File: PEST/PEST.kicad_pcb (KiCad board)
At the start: 4 copper layers, 6.2 x 4.9 mm, 4 parts, among them J1 Conn_01x01, J2 Conn_01x01, J3 Conn_01x01, J4 Conn_01x01

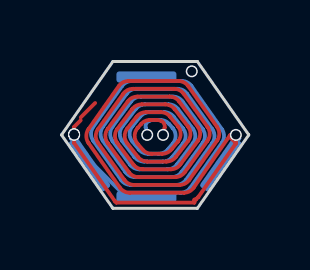
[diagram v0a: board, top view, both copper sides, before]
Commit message: Fixed some PEST tile glitches
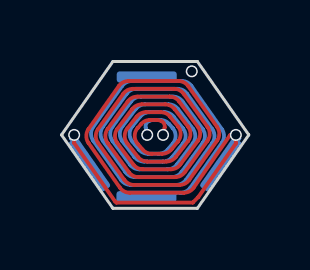
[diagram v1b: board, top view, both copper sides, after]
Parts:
- removed J3, J4: Conn_01x01, PEST:Bridge_Pad
- added J1: Conn_01x01, Touchstone:Bridge_Pad, B.Cu at (17.8, 21.0)
- added J2: Conn_01x01, Touchstone:Bridge_Pad, B.Cu at (19.7, 18.1)
- J1, J2: footprint PEST:Bridge_Pad -> Touchstone:Bridge_Pad
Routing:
- net Net-(J1-Pin_1): track 210.0 -> 206.4 mm, vias 6 -> 5
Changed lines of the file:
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@@
   (net 0 "")
   (net 1 "Net-(J1-Pin_1)")
-  (footprint "PEST:Bridge_Pad" (layer "B.Cu")
-    (at 19.71 18.07)
+  (footprint "Touchstone:Bridge_Pad" (layer "B.Cu")
+    (at 17.81 20.99 -55)
     (property "Sheetfile" "PEST.kicad_sch")
     (property "Sheetname" "")
@@
     (property "ki_keywords" "connector")
     (attr smd)
-    (fp_text reference "J4" (at -2.5 0.5 180 unlocked) (layer "B.SilkS") hide
+    (fp_text reference "J1" (at -2.5 0.5 125 unlocked) (layer "B.SilkS") hide
         (effects (font (size 1 1) (thickness 0.1)) (justify mirror))
     )
-    (fp_text value "Conn_01x01" (at 0 -1 180 unlocked) (layer "B.Fab")
+    (fp_text value "Conn_01x01" (at 0 -1 125 unlocked) (layer "B.Fab")
         (effects (font (size 1 1) (thickness 0.15)) (justify mirror))
     )
-    (fp_text user "${REFERENCE}" (at 0 -2.5 180 unlocked) (layer "B.Fab")
-        (effects (font (size 1 1) (thickness 0.15)) (justify mirror))
-    )
-    (pad "1" smd roundrect (at 0 0) (size 2 0.375) (layers "B.Cu" "B.Paste" "B.Mask") (roundrect_rratio 0.25)
+    (pad "1" smd roundrect (at 0 0 305) (size 2 0.375) (layers "B.Cu" "B.Paste" "B.Mask") (roundrect_rratio 0.25)
       (net 1 "Net-(J1-Pin_1)") (pinfunction "Pin_1") (pintype "passive") (thermal_bridge_angle 45))
   )
-  (footprint "PEST:Bridge_Pad" (layer "B.Cu")
+  (footprint "Touchstone:Bridge_Pad" (layer "B.Cu")
     (at 22.19 20.99 55)
     (property "Sheetfile" "PEST.kicad_sch")
@@
         (effects (font (size 1 1) (thickness 0.15)) (justify mirror))
     )
-    (fp_text user "${REFERENCE}" (at 0 -2.5 235 unlocked) (layer "B.Fab")
-        (effects (font (size 1 1) (thickness 0.15)) (justify mirror))
-    )
     (pad "1" smd roundrect (at 0 0 55) (size 2 0.375) (layers "B.Cu" "B.Paste" "B.Mask") (roundrect_rratio 0.25)
       (net 1 "Net-(J1-Pin_1)") (pinfunction "Pin_1") (pintype "passive") (thermal_bridge_angle 45))
   )
-  (footprint "PEST:Bridge_Pad" (layer "B.Cu")
-    (at 17.81 20.99 -55)
+  (footprint "Touchstone:Bridge_Pad" (layer "B.Cu")
+    (at 19.72 18.07 180)
     (property "Sheetfile" "PEST.kicad_sch")
     (property "Sheetname" "")
@@
     (property "ki_keywords" "connector")
     (attr smd)
-    (fp_text reference "J3" (at -2.5 0.5 125 unlocked) (layer "B.SilkS") hide
+    (fp_text reference "J2" (at -2.5 0.5 unlocked) (layer "B.SilkS") hide
         (effects (font (size 1 1) (thickness 0.1)) (justify mirror))
     )
-    (fp_text value "Conn_01x01" (at 0 -1 125 unlocked) (layer "B.Fab")
+    (fp_text value "Conn_01x01" (at 0 -1 unlocked) (layer "B.Fab") hide
         (effects (font (size 1 1) (thickness 0.15)) (justify mirror))
     )
-    (fp_text user "${REFERENCE}" (at 0 -2.5 125 unlocked) (layer "B.Fab")
-        (effects (font (size 1 1) (thickness 0.15)) (justify mirror))
-    )
-    (pad "1" smd roundrect (at 0 0 305) (size 2 0.375) (layers "B.Cu" "B.Paste" "B.Mask") (roundrect_rratio 0.25)
+    (pad "1" smd roundrect (at 0 0 180) (size 2 0.375) (layers "B.Cu" "B.Paste" "B.Mask") (roundrect_rratio 0.25)
       (net 1 "Net-(J1-Pin_1)") (pinfunction "Pin_1") (pintype "passive") (thermal_bridge_angle 45))
   )
-  (footprint "PEST:Bridge_Pad" (layer "B.Cu")
+  (footprint "Touchstone:Bridge_Pad" (layer "B.Cu")
     (at 19.71 22.06 180)
     (property "Sheetfile" "PEST.kicad_sch")
@@
         (effects (font (size 1 1) (thickness 0.1)) (justify mirror))
     )
-    (fp_text value "Conn_01x01" (at 0 -1 unlocked) (layer "B.Fab")
-        (effects (font (size 1 1) (thickness 0.15)) (justify mirror))
-    )
-    (fp_text user "${REFERENCE}" (at 0 -2.5 unlocked) (layer "B.Fab")
+    (fp_text value "Conn_01x01" (at 0 -1 unlocked) (layer "B.Fab") hide
         (effects (font (size 1 1) (thickness 0.15)) (justify mirror))
     )
@@
   (segment (start 20.186928 19.242228) (end 19.696407 19.242228) (width 0.127) (layer "F.Cu") (net 1))
   (segment (start 19.740993 20.887676) (end 20.374247 20.887676) (width 0.127) (layer "F.Cu") (net 1))
-  (segment (start 22.69 20.284244) (end 22.69 20) (width 0.127) (layer "F.Cu") (net 1))
+  (segment (start 18.7065 22.2565) (end 21.2535 22.2565) (width 0.127) (layer "F.Cu") (net 1))
+  (segment (start 18.654759 22.204759) (end 18.7065 22.2565) (width 0.127) (layer "F.Cu") (net 1))
   (segment (start 19.234799 19.141489) (end 18.741901 19.794714) (width 0.127) (layer "F.Cu") (net 1))
   (segment (start 19.884096 20.627868) (end 20.234467 20.627868) (width 0.127) (layer "F.Cu") (net 1))
-  (segment (start 22.503 20.083) (end 22.69 20.27) (width 0.127) (layer "F.Cu") (net 1))
   (segment (start 20.774858 18.202997) (end 19.114606 18.202997) (width 0.127) (layer "F.Cu") (net 1))
-  (segment (start 17.3 20.269963) (end 18.654759 22.204759) (width 0.127) (layer "F.Cu") (net 1))
   (segment (start 20.69099 20.731958) (end 21.094195 20.209152) (width 0.127) (layer "F.Cu") (net 1))
   (segment (start 20.988534 21.241539) (end 21.742858 20.197439) (width 0.127) (layer "F.Cu") (net 1))
-  (segment (start 17.295147 19.974079) (end 17.295147 19.736968) (width 0.127) (layer "F.Cu") (net 1))
+  (segment (start 17.3 20.269963) (end 18.654759 22.204759) (width 0.127) (layer "F.Cu") (net 1))
   (segment (start 19.530266 19.639617) (end 19.416309 19.770713) (width 0.127) (layer "F.Cu") (net 1))
   (segment (start 20.760556 19.713911) (end 20.497376 19.389993) (width 0.127) (layer "F.Cu") (net 1))
-  (segment (start 17.295147 19.736968) (end 17.52 19.512115) (width 0.127) (layer "F.Cu") (net 1))
   (segment (start 20.478584 18.722613) (end 19.408912 18.722613) (width 0.127) (layer "F.Cu") (net 1))
   (segment (start 20.046604 19.502035) (end 19.832154 19.502035) (width 0.127) (layer "F.Cu") (net 1))
@@
   (segment (start 19.070581 20.281561) (end 19.426387 20.734704) (width 0.127) (layer "F.Cu") (net 1))
   (segment (start 19.38304 19.39363) (end 19.07182 19.785935) (width 0.127) (layer "F.Cu") (net 1))
-  (segment (start 18.7065 22.2565) (end 21.309012 22.2565) (width 0.127) (layer "F.Cu") (net 1))
-  (segment (start 21.309012 22.155867) (end 21.354133 22.155867) (width 0.127) (layer "F.Cu") (net 1))
+  (segment (start 17.3 20) (end 17.3 20.269963) (width 0.127) (layer "F.Cu") (net 1))
   (segment (start 21.743247 19.729484) (end 20.951045 18.629098) (width 0.127) (layer "F.Cu") (net 1))
-  (segment (start 21.309012 22.2565) (end 21.309012 22.155867) (width 0.127) (layer "F.Cu") (net 1))
   (segment (start 19.150771 21.926907) (end 20.958062 21.926907) (width 0.127) (layer "F.Cu") (net 1))
   (segment (start 22.503 20) (end 22.69 20) (width 0.127) (layer "F.Cu") (net 1))
   (segment (start 20.626421 18.462805) (end 19.262208 18.462805) (width 0.127) (layer "F.Cu") (net 1))
   (segment (start 21.095122 19.721794) (end 20.649442 19.139345) (width 0.127) (layer "F.Cu") (net 1))
-  (segment (start 17.3 20) (end 17.3 20.269963) (width 0.127) (layer "F.Cu") (net 1))
+  (segment (start 21.2535 22.2565) (end 21.438667 22.071333) (width 0.127) (layer "F.Cu") (net 1))
+  (segment (start 22.69 20.284244) (end 22.69 20) (width 0.127) (layer "F.Cu") (net 1))
   (segment (start 20.315386 19.75731) (end 20.264 20) (width 0.127) (layer "F.Cu") (net 1))
-  (segment (start 21.438667 22.071333) (end 22.69 20.284244) (width 0.127) (layer "F.Cu") (net 1))
   (segment (start 21.421164 19.726432) (end 20.80046 18.885135) (width 0.127) (layer "F.Cu") (net 1))
   (segment (start 18.417445 20.271899) (end 19.124211 21.242716) (width 0.127) (layer "F.Cu") (net 1))
@@
   (segment (start 18.741181 20.27562) (end 19.274971 20.987458) (width 0.127) (layer "F.Cu") (net 1))
   (segment (start 21.137783 21.498492) (end 22.062894 20.194033) (width 0.127) (layer "F.Cu") (net 1))
-  (segment (start 17.52 19.415845) (end 18 18.935845) (width 0.127) (layer "F.Cu") (net 1))
+  (segment (start 21.438667 22.071333) (end 22.69 20.284244) (width 0.127) (layer "F.Cu") (net 1))
   (segment (start 18.787523 18.372744) (end 17.777627 19.807337) (width 0.127) (layer "F.Cu") (net 1))
   (segment (start 20.839548 20.985738) (end 21.420589 20.202164) (width 0.127) (layer "F.Cu") (net 1))
   (segment (start 18.936868 18.630095) (end 18.096915 19.804392) (width 0.127) (layer "F.Cu") (net 1))
   (segment (start 19.086 18.886545) (end 18.417914 19.800407) (width 0.127) (layer "F.Cu") (net 1))
-  (segment (start 21.354133 22.155867) (end 21.438667 22.071333) (width 0.127) (layer "F.Cu") (net 1))
   (segment (start 20.543177 20.482226) (end 20.758819 20.220504) (width 0.127) (layer "F.Cu") (net 1))
   (segment (start 21.286821 21.754761) (end 22.503 20) (width 0.127) (layer "F.Cu") (net 1))
   (segment (start 19.59499 21.147484) (end 20.518246 21.147484) (width 0.127) (layer "F.Cu") (net 1))
   (segment (start 22.063175 19.731644) (end 21.101418 18.372002) (width 0.127) (layer "F.Cu") (net 1))
-  (segment (start 18.654759 22.204759) (end 18.7065 22.2565) (width 0.127) (layer "F.Cu") (net 1))
   (segment (start 18.096586 20.269351) (end 18.973749 21.499348) (width 0.127) (layer "F.Cu") (net 1))
   (segment (start 19.413709 20.292529) (end 19.579608 20.487266) (width 0.127) (layer "F.Cu") (net 1))
-  (via (at 17.295147 19.974079) (size 0.4) (drill 0.3) (layers "F.Cu" "B.Cu") (net 1))
   (via (at 19.736 20) (size 0.4) (drill 0.3) (layers "F.Cu" "B.Cu") (net 1))
   (via (at 22.69 20) (size 0.4) (drill 0.3) (layers "F.Cu" "B.Cu") (net 1))
@@
   (segment (start 17.462194 20.5016) (end 17.295147 20.263032) (width 0.127) (layer "B.Cu") (net 1))
   (segment (start 20.259007 20.887676) (end 19.625753 20.887676) (width 0.127) (layer "B.Cu") (net 1))
-  (segment (start 18.8875 21.926906) (end 17.462194 20.5016) (width 0.127) (layer "B.Cu") (net 1))
   (segment (start 20.61696 19.39363) (end 20.92818 19.785935) (width 0.127) (layer "B.Cu") (net 1))
   (segment (start 17.3 20) (end 17.188819 20.111181) (width 0.127) (layer "B.Cu") (net 1))

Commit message: Reduced PEST tile to two pins, added SMD footprint
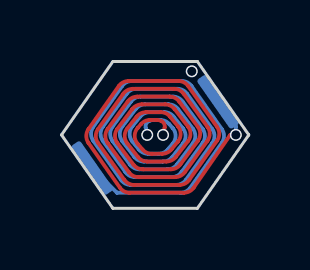
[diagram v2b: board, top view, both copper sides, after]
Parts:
- removed J1 (x2), J2 (x2): Conn_01x01, Touchstone:Bridge_Pad
- added REF**: PEST_Tile, Touchstone:PEST_Tile, F.Cu at (20.0, 20.0)
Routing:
- net Net-(J1-Pin_1): track 206.4 -> 198.0 mm, vias 5 -> 4

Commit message: Finalized PCBs for fabrication
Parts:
- moved REF** 28.3 mm to (0.00, 0.00)
